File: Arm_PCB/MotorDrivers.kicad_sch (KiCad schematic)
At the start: 54 parts, among them J12 Conn_02x03_Counter_Clockwise, J13 Conn_02x03_Counter_Clockwise, U0 INA219AxDCN, U0 TB6560_Board, U1 INA219AxDCN, U1 TB6560_Board, U2 INA219AxDCN, U2 TB6560_Board, U3 INA219AxDCN, U3 TB6560_Board, U4 INA219AxDCN, U4 TB6560_Board, U5 INA219AxDCN, U5 TB6560_Board, U6 INA219AxDCN, U6 TB6560_Board, U7 INA219AxDCN, U8 INA219AxDCN

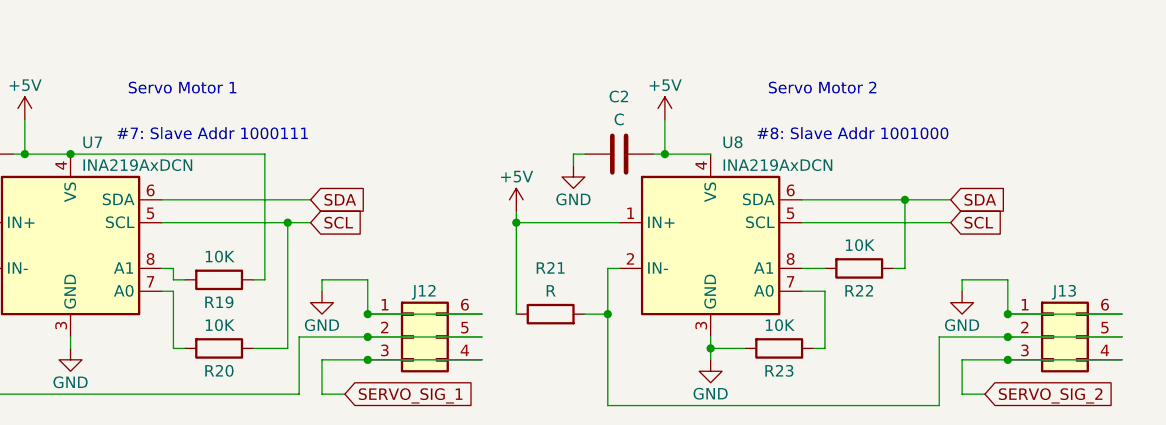
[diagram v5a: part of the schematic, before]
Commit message: Update footprint library
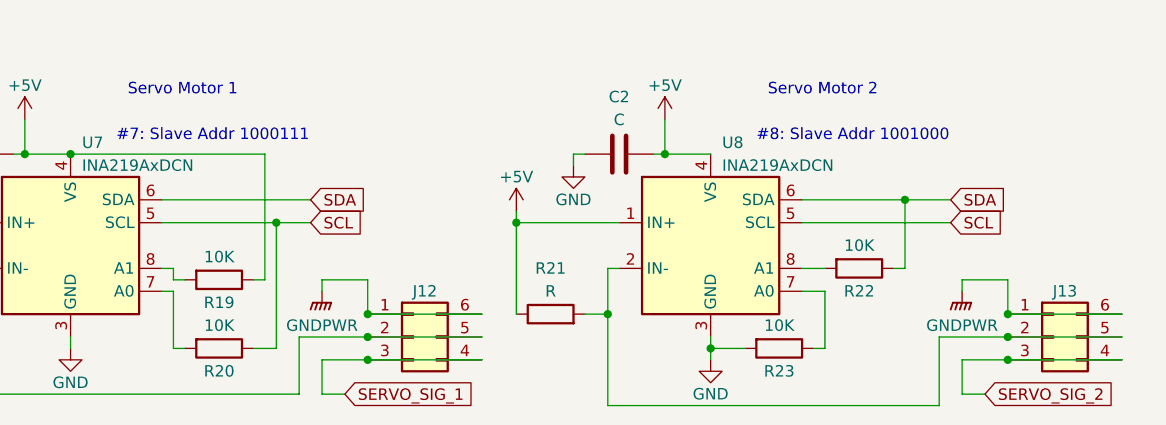
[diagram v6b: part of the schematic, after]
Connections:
- net GND: no longer J12.1 (Pin_1), J12.6 (Pin_6), J13.1 (Pin_1), J13.6 (Pin_6)
- net GNDPWR: now also J12.1 (Pin_1), J12.6 (Pin_6), J13.1 (Pin_1), J13.6 (Pin_6)
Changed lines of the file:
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@@
   (junction (at 22.86 127) (diameter 0) (color 0 0 0 0)
   )
+  (junction (at 60.96 179.07) (diameter 0) (color 0 0 0 0)
+  )
   (junction (at 130.81 176.53) (diameter 0) (color 0 0 0 0)
   )
   (junction (at 104.14 171.45) (diameter 0) (color 0 0 0 0)
   )
-  (junction (at 62.23 179.07) (diameter 0) (color 0 0 0 0)
-  )
   (junction (at 52.07 43.18) (diameter 0) (color 0 0 0 0)
   )
@@
     (stroke (width 0) (type default))
   )
-  (wire (pts (xy 62.23 179.07) (xy 62.23 193.04))
+  (wire (pts (xy 60.96 179.07) (xy 60.96 193.04))
     (stroke (width 0) (type default))
   )
@@
     (stroke (width 0) (type default))
   )
-  (wire (pts (xy 58.42 193.04) (xy 62.23 193.04))
+  (wire (pts (xy 58.42 193.04) (xy 60.96 193.04))
     (stroke (width 0) (type default))
   )
@@
     (stroke (width 0) (type default))
   )
-  (wire (pts (xy 62.23 179.07) (xy 64.77 179.07))
-    (stroke (width 0) (type default))
-  )
   (wire (pts (xy 76.2 86.36) (xy 76.2 90.17))
     (stroke (width 0) (type default))
@@
     (stroke (width 0) (type default))
   )
-  (wire (pts (xy 48.26 179.07) (xy 62.23 179.07))
+  (wire (pts (xy 48.26 179.07) (xy 60.96 179.07))
     (stroke (width 0) (type default))
   )
@@
     (stroke (width 0) (type default))
   )
+  (wire (pts (xy 60.96 179.07) (xy 64.77 179.07))
+    (stroke (width 0) (type default))
+  )
   (wire (pts (xy 137.16 194.31) (xy 137.16 198.12))
     (stroke (width 0) (type default))
@@
     )
   )
+  (symbol (lib_name "GNDPWR_1") (lib_id "power:GNDPWR") (at 66.04 186.69 0) (unit 1)
+    (in_bom yes) (on_board yes) (dnp no)
+    (property "Reference" "#PWR018" (at 66.04 191.77 0)
+      (effects (font (size 1.27 1.27)) hide)
+    )
+    (property "Value" "GNDPWR" (at 66.04 190.5 0)
+      (effects (font (size 1.27 1.27)))
+    )
+    (property "Footprint" "" (at 66.04 187.96 0)
+      (effects (font (size 1.27 1.27)) hide)
+    )
+    (property "Datasheet" "" (at 66.04 187.96 0)
+      (effects (font (size 1.27 1.27)) hide)
+    )
+    (pin "1")
+    (instances
+      (project "Arm_PCB"
+        (path "/f8b9fbb1-757f-4aa8-8e30-7f83a30c7c5f/bb228902-3eef-4db7-9bf2-e6e1028f63fe"
+          (reference "#PWR018") (unit 1)
+        )
+      )
+    )
+  )
   (symbol (lib_id "power:GND") (at 38.1 193.04 0) (unit 1)
     (in_bom yes) (on_board yes) (dnp no)
@@
     )
   )
-  (symbol (lib_id "power:GND") (at 137.16 186.69 0) (unit 1)
-    (in_bom yes) (on_board yes) (dnp no)
-    (property "Reference" "#PWR027" (at 137.16 193.04 0)
-      (effects (font (size 1.27 1.27)) hide)
-    )
-    (property "Value" "GND" (at 137.16 190.5 0)
-      (effects (font (size 1.27 1.27)))
-    )
-    (property "Footprint" "" (at 137.16 186.69 0)
-      (effects (font (size 1.27 1.27)) hide)
-    )
-    (property "Datasheet" "" (at 137.16 186.69 0)
-      (effects (font (size 1.27 1.27)) hide)
-    )
-    (pin "1")
-    (instances
-      (project "Arm_PCB"
-        (path "/f8b9fbb1-757f-4aa8-8e30-7f83a30c7c5f/bb228902-3eef-4db7-9bf2-e6e1028f63fe"
-          (reference "#PWR027") (unit 1)
-        )
-      )
-    )
-  )
   (symbol (lib_id "power:GND") (at 125.73 48.26 0) (unit 1)
     (in_bom yes) (on_board yes) (dnp no) (fields_autoplaced)
@@
     )
   )
-  (symbol (lib_id "power:GND") (at 66.04 186.69 0) (unit 1)
-    (in_bom yes) (on_board yes) (dnp no)
-    (property "Reference" "#PWR018" (at 66.04 193.04 0)
-      (effects (font (size 1.27 1.27)) hide)
-    )
-    (property "Value" "GND" (at 66.04 190.5 0)
-      (effects (font (size 1.27 1.27)))
-    )
-    (property "Footprint" "" (at 66.04 186.69 0)
-      (effects (font (size 1.27 1.27)) hide)
-    )
-    (property "Datasheet" "" (at 66.04 186.69 0)
-      (effects (font (size 1.27 1.27)) hide)
-    )
-    (pin "1")
-    (instances
-      (project "Arm_PCB"
-        (path "/f8b9fbb1-757f-4aa8-8e30-7f83a30c7c5f/bb228902-3eef-4db7-9bf2-e6e1028f63fe"
-          (reference "#PWR018") (unit 1)
-        )
-      )
-    )
-  )
   (symbol (lib_id "Device:R") (at 91.44 189.23 90) (unit 1)
     (in_bom yes) (on_board yes) (dnp no)
@@
         )
       )
+    )
+  )
+  (symbol (lib_name "GNDPWR_1") (lib_id "power:GNDPWR") (at 137.16 186.69 0) (unit 1)
+    (in_bom yes) (on_board yes) (dnp no)
+    (property "Reference" "#PWR027" (at 137.16 191.77 0)
+      (effects (font (size 1.27 1.27)) hide)
+    )
+    (property "Value" "GNDPWR" (at 137.16 190.5 0)
+      (effects (font (size 1.27 1.27)))
+    )
+    (property "Footprint" "" (at 137.16 187.96 0)
+      (effects (font (size 1.27 1.27)) hide)
+    )
+    (property "Datasheet" "" (at 137.16 187.96 0)
+      (effects (font (size 1.27 1.27)) hide)
+    )
+    (pin "1")
+    (instances
+      (project "Arm_PCB"
+        (path "/f8b9fbb1-757f-4aa8-8e30-7f83a30c7c5f/bb228902-3eef-4db7-9bf2-e6e1028f63fe"
+          (reference "#PWR027") (unit 1)
+        )
+      )

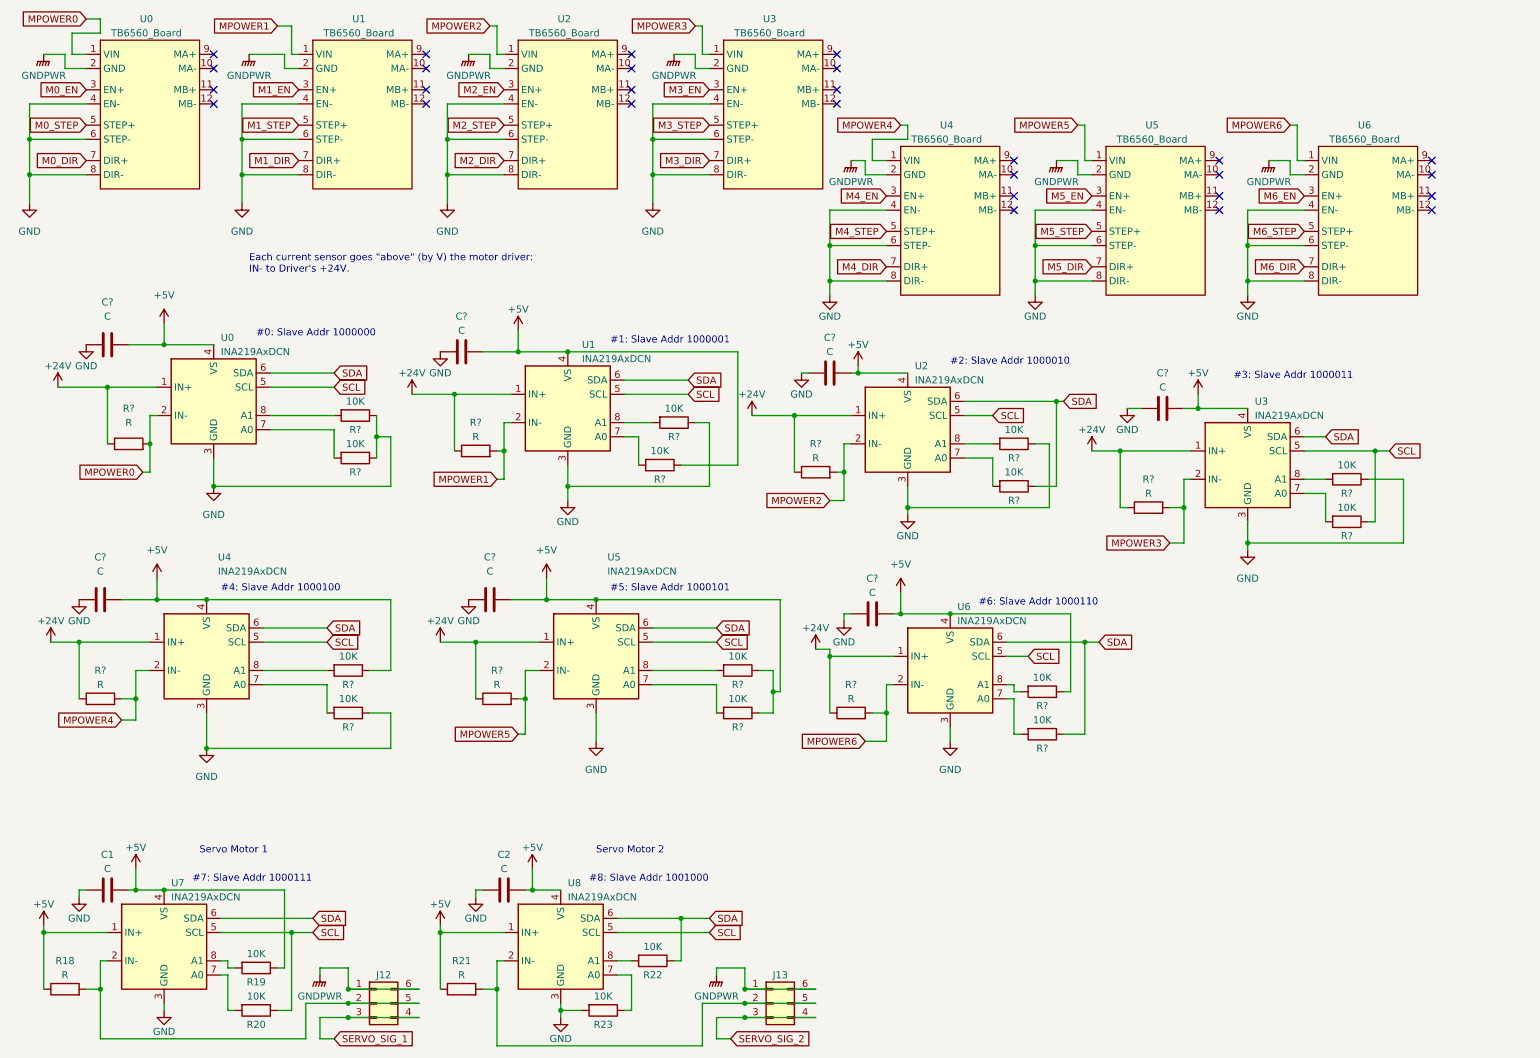
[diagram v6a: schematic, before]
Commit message: Annotate all pages
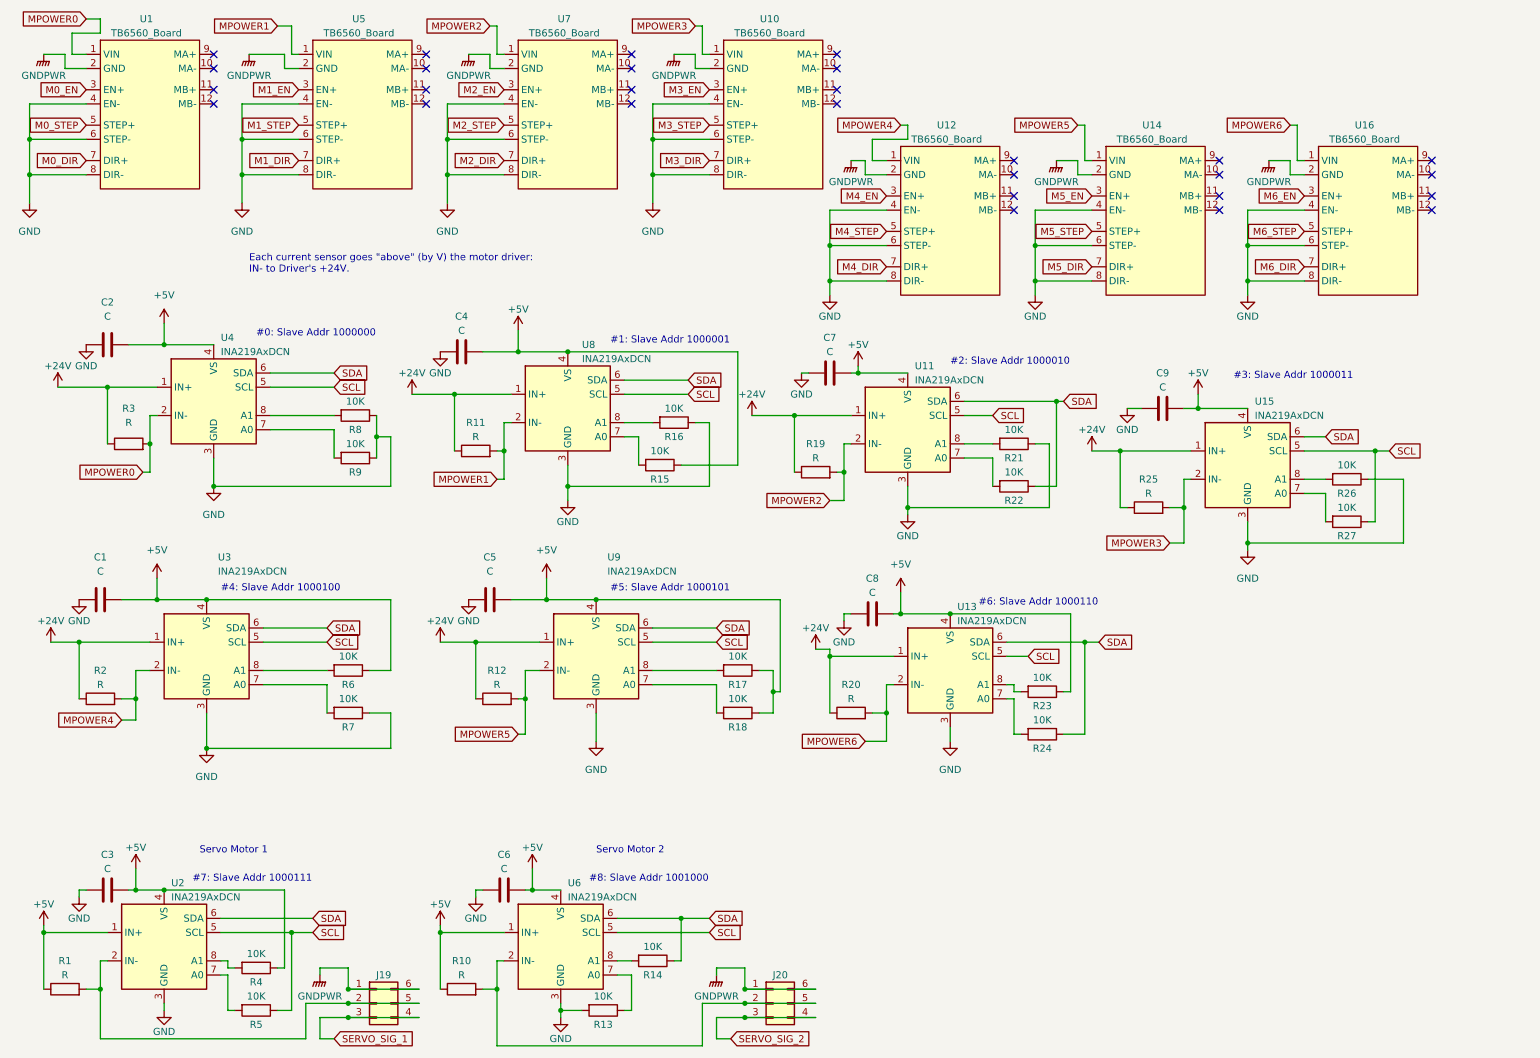
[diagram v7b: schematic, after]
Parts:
- gave numbers to parts that had none: 28
- renumbered C1 to C3, C2 to C6, J12 to J19, J13 to J20, R18 to R1, R21 to R10, R23 to R13, R22 to R14, R19 to R4, R20 to R5, U0 to U1, U3 to U10, U2 to U11, U4 to U12, U6 to U13, U5 to U14, U3 to U15, U6 to U16, U7 to U2, U4 to U3, U0 to U4, U1 to U5, U8 to U6, U2 to U7, U1 to U8, U5 to U9
